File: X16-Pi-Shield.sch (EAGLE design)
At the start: 40 parts, among them J1 CONN_DF13-4P-1.25DSA, J3 CONN_DF13-4P-1.25DSA, J4 HTST-110-04-L-D-RA, J5 BM04B-GHS-TBT, J6 BM04B-GHS-TBT, U1 INA260AIPW, U2 AZ1117IH-3.3TRG1

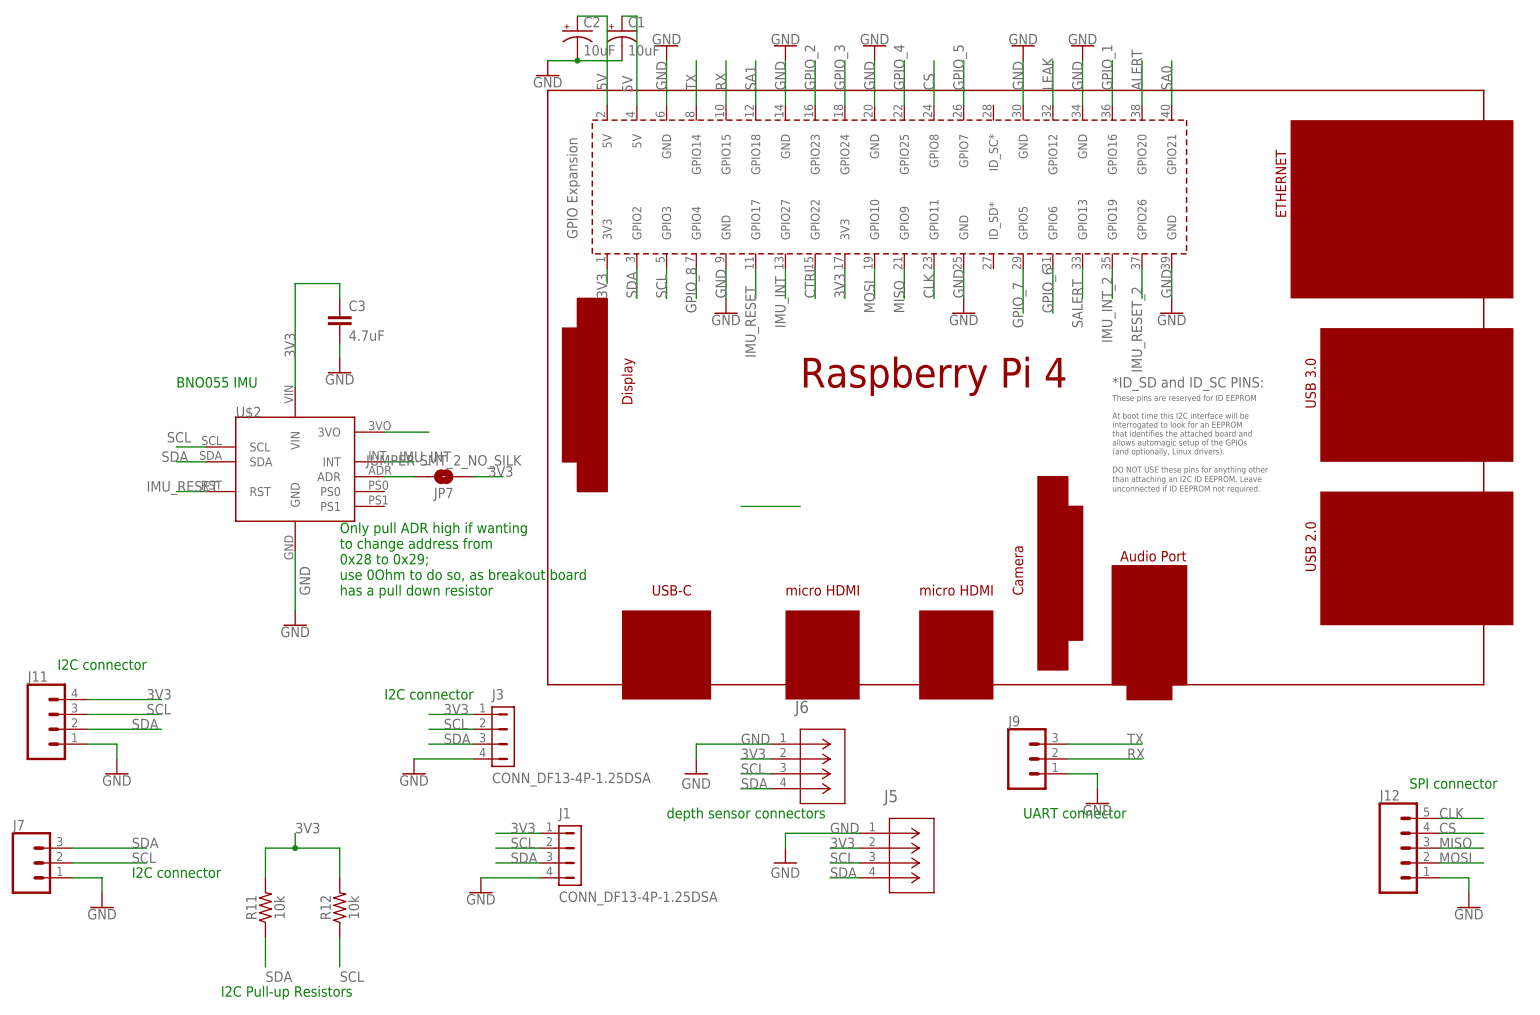
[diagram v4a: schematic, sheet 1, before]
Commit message: Minh Update 4 - Edit PMBUS traces, and modify Label + Traces
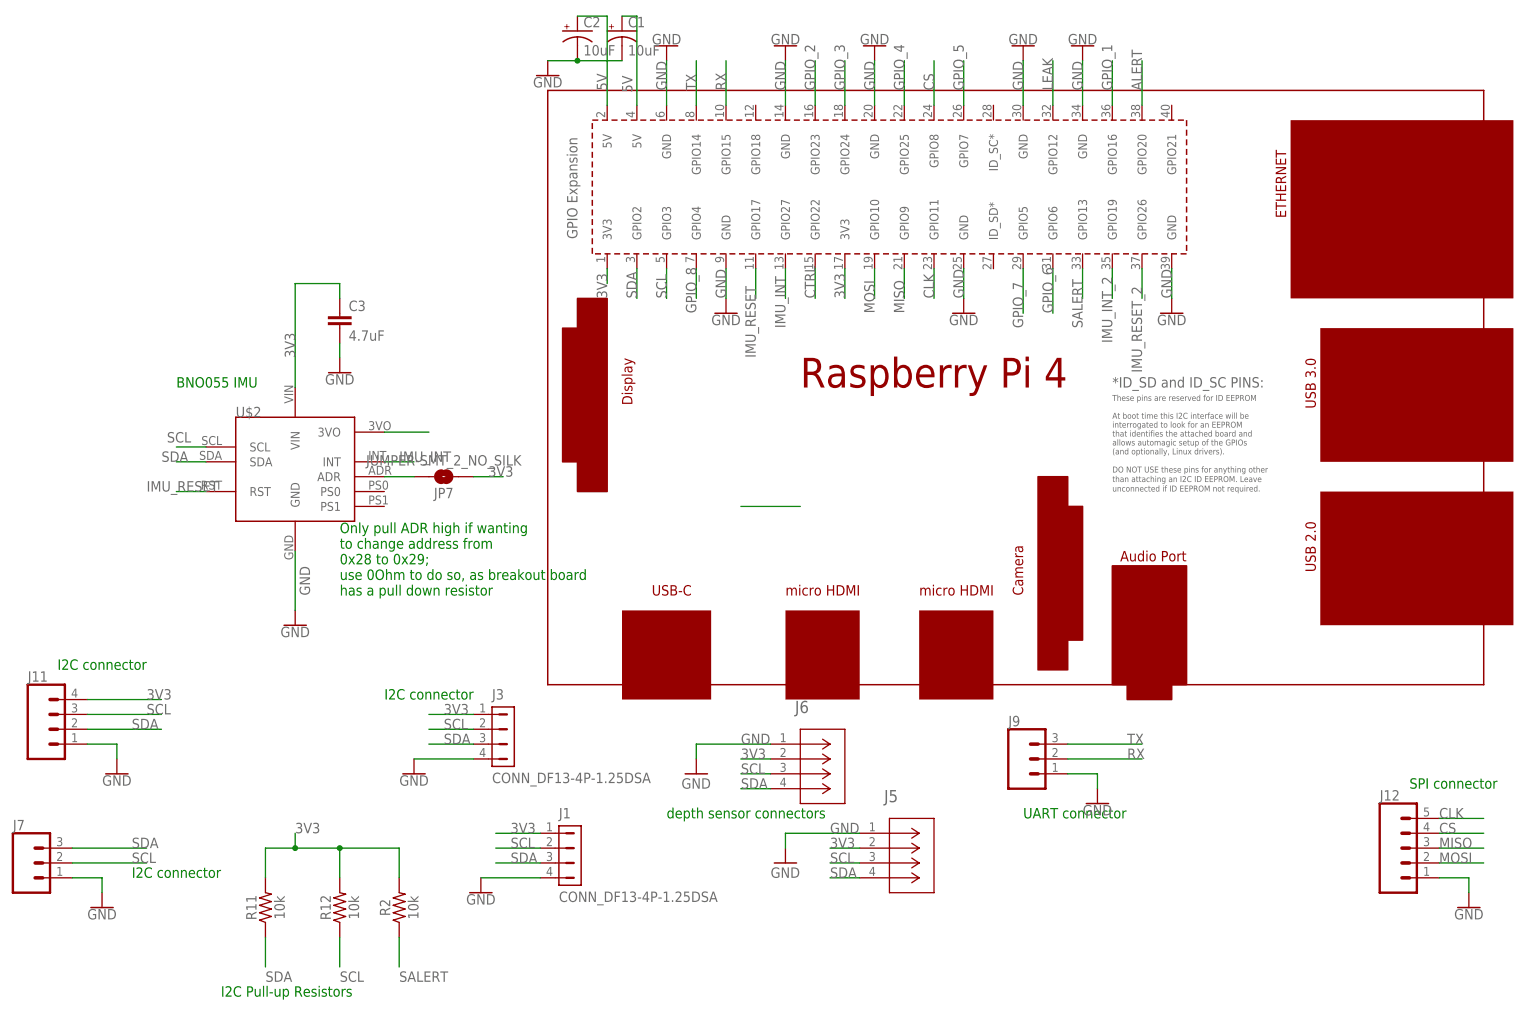
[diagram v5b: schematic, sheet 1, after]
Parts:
- added R2: 10k, SparkFun-Resistors:RESISTOR0603
- C4: value 2.2uF -> 10uF
- C5: value 2.2uF -> 22uF
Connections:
- removed net SA0: J4.2, U$1.GPIO21
- removed net SA1: J4.15, U$1.GPIO18
- net 3V3: now also R2.2
- net SALERT: now also R2.1
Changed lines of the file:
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@@
 <part name="U2" library="X16-Pi-Shield" deviceset="AZ1117IH-3.3TRG1" device=""/>
 <part name="GND17" library="SparkFun-PowerSymbols" library_urn="urn:adsk.eagle:library:530" deviceset="GND" device=""/>
-<part name="C4" library="SparkFun-Capacitors" library_urn="urn:adsk.eagle:library:510" deviceset="2.2UF" device="-0603-10V-20%" package3d_urn="urn:adsk.eagle:package:37414/1" value="2.2uF"/>
-<part name="C5" library="SparkFun-Capacitors" library_urn="urn:adsk.eagle:library:510" deviceset="2.2UF" device="-0603-10V-20%" package3d_urn="urn:adsk.eagle:package:37414/1" value="2.2uF"/>
+<part name="C4" library="SparkFun-Capacitors" library_urn="urn:adsk.eagle:library:510" deviceset="2.2UF" device="-0603-10V-20%" package3d_urn="urn:adsk.eagle:package:37414/1" value="10uF"/>
+<part name="C5" library="SparkFun-Capacitors" library_urn="urn:adsk.eagle:library:510" deviceset="2.2UF" device="-0603-10V-20%" package3d_urn="urn:adsk.eagle:package:37414/1" value="22uF"/>
 <part name="GND18" library="SparkFun-PowerSymbols" library_urn="urn:adsk.eagle:library:530" deviceset="GND" device=""/>
 <part name="GND19" library="SparkFun-PowerSymbols" library_urn="urn:adsk.eagle:library:530" deviceset="GND" device=""/>
@@
 <part name="R1" library="SparkFun-Resistors" library_urn="urn:adsk.eagle:library:532" deviceset="RESISTOR" device="0603" package3d_urn="urn:adsk.eagle:package:39650/1" value="250"/>
 <part name="GND24" library="SparkFun-PowerSymbols" library_urn="urn:adsk.eagle:library:530" deviceset="GND" device=""/>
+<part name="R2" library="SparkFun-Resistors" library_urn="urn:adsk.eagle:library:532" deviceset="RESISTOR" device="0603" package3d_urn="urn:adsk.eagle:package:39650/1" value="10k"/>
 </parts>
 <sheets>
@@
 <attribute name="VALUE" x="127" y="43.18" size="1.778" layer="96"/>
 </instance>
+<instance part="R2" gate="G$1" x="78.74" y="22.86" smashed="yes" rot="R90">
+<attribute name="NAME" x="77.216" y="22.86" size="1.778" layer="95" font="vector" rot="R90" align="bottom-center"/>
+<attribute name="VALUE" x="80.264" y="22.86" size="1.778" layer="96" font="vector" rot="R90" align="top-center"/>
+</instance>
 </instances>
 <busses>
@@
 <junction x="60.96" y="33.02"/>
 <label x="60.96" y="35.56" size="1.778" layer="95"/>
+<pinref part="R2" gate="G$1" pin="2"/>
+<wire x1="68.58" y1="33.02" x2="78.74" y2="33.02" width="0.1524" layer="91"/>
+<wire x1="78.74" y1="33.02" x2="78.74" y2="27.94" width="0.1524" layer="91"/>
+<junction x="68.58" y="33.02"/>
 </segment>
 <segment>
@@
 <label x="195.58" y="121.92" size="1.778" layer="95" rot="R90"/>
 </segment>
-</net>
-<net name="SA1" class="0">
-<segment>
-<pinref part="U$1" gate="G$1" pin="GPIO18"/>
-<wire x1="139.7" y1="160.02" x2="139.7" y2="167.64" width="0.1524" layer="91"/>
-<label x="139.7" y="162.56" size="1.778" layer="95" rot="R90"/>
-</segment>
-</net>
-<net name="SA0" class="0">
-<segment>
-<pinref part="U$1" gate="G$1" pin="GPIO21"/>
-<wire x1="210.82" y1="160.02" x2="210.82" y2="167.64" width="0.1524" layer="91"/>
-<label x="210.82" y="162.56" size="1.778" layer="95" rot="R90"/>
+<segment>
+<pinref part="R2" gate="G$1" pin="1"/>
+<wire x1="78.74" y1="17.78" x2="78.74" y2="12.7" width="0.1524" layer="91"/>
+<label x="78.74" y="10.16" size="1.778" layer="95"/>
 </segment>
 </net>
@@
 </busses>
 <nets>
-<net name="SA0" class="0">
-<segment>
-<pinref part="J4" gate="A" pin="2"/>
-<wire x1="60.96" y1="105.41" x2="49.53" y2="105.41" width="0.1524" layer="91"/>
-<label x="49.53" y="105.41" size="1.778" layer="95"/>
-</segment>
-</net>
 <net name="GPIO_1" class="0">
 <segment>
@@
 </segment>
 </net>
-<net name="SA1" class="0">
-<segment>
-<pinref part="J4" gate="A" pin="15"/>
-<wire x1="60.96" y1="72.39" x2="49.53" y2="72.39" width="0.1524" layer="91"/>
-<label x="49.53" y="72.39" size="1.778" layer="95"/>
-</segment>
-</net>

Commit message: Minh Update 5
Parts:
- renumbered 3V to 3V_LED, 5V to 5V_LED
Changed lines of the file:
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@@
 <part name="GND29" library="SparkFun-PowerSymbols" library_urn="urn:adsk.eagle:library:530" deviceset="GND" device=""/>
 <part name="FRAME2" library="SparkFun-Aesthetics" deviceset="FRAME-A4L" device=""/>
-<part name="5V" library="led" library_urn="urn:adsk.eagle:library:259" deviceset="LED" device="CHIPLED_0805" package3d_urn="urn:adsk.eagle:package:15821/2"/>
-<part name="3V" library="led" library_urn="urn:adsk.eagle:library:259" deviceset="LED" device="CHIPLED_0805" package3d_urn="urn:adsk.eagle:package:15821/2"/>
+<part name="5V_LED" library="led" library_urn="urn:adsk.eagle:library:259" deviceset="LED" device="CHIPLED_0805" package3d_urn="urn:adsk.eagle:package:15821/2"/>
+<part name="3V_LED" library="led" library_urn="urn:adsk.eagle:library:259" deviceset="LED" device="CHIPLED_0805" package3d_urn="urn:adsk.eagle:package:15821/2"/>
 <part name="R15" library="SparkFun-Resistors" library_urn="urn:adsk.eagle:library:532" deviceset="RESISTOR" device="0603" package3d_urn="urn:adsk.eagle:package:39650/1" value="250"/>
 <part name="R16" library="SparkFun-Resistors" library_urn="urn:adsk.eagle:library:532" deviceset="RESISTOR" device="0603" package3d_urn="urn:adsk.eagle:package:39650/1" value="150"/>
@@
 <attribute name="DESIGNER" x="226.26" y="6.35" size="2.54" layer="94" font="vector"/>
 </instance>
-<instance part="5V" gate="G$1" x="157.48" y="71.12" smashed="yes">
+<instance part="5V_LED" gate="G$1" x="157.48" y="71.12" smashed="yes">
 <attribute name="NAME" x="154.051" y="66.548" size="1.778" layer="95" font="vector" rot="R90"/>
 <attribute name="VALUE" x="159.385" y="66.548" size="1.778" layer="96" font="vector" rot="R90" align="top-left"/>
 </instance>
-<instance part="3V" gate="G$1" x="172.72" y="71.12" smashed="yes">
+<instance part="3V_LED" gate="G$1" x="172.72" y="71.12" smashed="yes">
 <attribute name="NAME" x="169.291" y="66.548" size="1.778" layer="95" font="vector" rot="R90"/>
 <attribute name="VALUE" x="174.625" y="66.548" size="1.778" layer="96" font="vector" rot="R90" align="top-left"/>
@@
 <segment>
 <pinref part="R15" gate="G$1" pin="1"/>
-<pinref part="5V" gate="G$1" pin="A"/>
+<pinref part="5V_LED" gate="G$1" pin="A"/>
 <wire x1="157.48" y1="83.82" x2="157.48" y2="73.66" width="0.1524" layer="91"/>
 </segment>
@@
 <segment>
 <pinref part="R16" gate="G$1" pin="1"/>
-<pinref part="3V" gate="G$1" pin="A"/>
+<pinref part="3V_LED" gate="G$1" pin="A"/>
 <wire x1="172.72" y1="83.82" x2="172.72" y2="73.66" width="0.1524" layer="91"/>
 </segment>
@@
 <net name="GND" class="0">
 <segment>
-<pinref part="3V" gate="G$1" pin="C"/>
+<pinref part="3V_LED" gate="G$1" pin="C"/>
 <wire x1="172.72" y1="66.04" x2="172.72" y2="63.5" width="0.1524" layer="91"/>
 <pinref part="GND44" gate="1" pin="GND"/>
 </segment>
 <segment>
-<pinref part="5V" gate="G$1" pin="C"/>
+<pinref part="5V_LED" gate="G$1" pin="C"/>
 <wire x1="157.48" y1="66.04" x2="157.48" y2="63.5" width="0.1524" layer="91"/>
 <pinref part="GND43" gate="1" pin="GND"/>
